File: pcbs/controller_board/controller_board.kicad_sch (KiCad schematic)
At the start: 28 parts, among them J1 A-2014-2-4-N-T-R, J2 PINHD-1X7, J3 PINHD-1X12, J4 PINHD-1X4, P1 PJ-064A, U1 R-78E5.0-1.0, U2 PHOTON2, U3 BSS138, U4 BSS138, U5 BSS138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

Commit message: update controller board to version 0.73
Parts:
- D1: value SS36 -> 3A/60V/750mV; footprint footprints:D_SS36 -> footprints:D_DO-214AB_SMC; symbol symbols:D_SS36 -> symbols:D_Schottky_3A_60V_750mV; DigiKeyURL (none) -> https://www.digikey.com/en/products/detail/onsemi/SS36/1053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; MPN (none) -> SS36; URL https://www.digikey.com/en/products/detail/onsemi/SS36/1053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 -> (none)
- D2: value SS36 -> 1A/40V/500mV; footprint footprints:D_SS36 -> footprints:D_DO-214AC_SMA; symbol symbols:D_SS36 -> symbols:D_Schottky_1A_40V_500mV; DigiKey SS36FSCT-ND -> SS14CT-ND; DigiKeyURL (none) -> https://www.digikey.com/en/products/detail/onsemi/SS14/9654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; MPN (none) -> SS14; URL https://www.digikey.com/en/products/detail/onsemi/SS36/1053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 -> (none)
- D3: value SMBJ36A -> 40V; footprint footprints:TVS_SMBJ36A -> footprints:D_DO-214AA_SMB; symbol symbols:TVS_SMBJ36A -> symbols:D_Zener_40V; DigiKeyURL (none) -> https://www.digikey.com/en/products/detail/littelfuse-inc/S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; MPN (none) -> SMBJ36A; URL https://www.digikey.com/en/products/detail/littelfuse-inc/S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 -> (none)
- F1: value PFSM.075.2 -> 33V/750mA/1.5A; footprint footprints:POLYFUSE_SMD075F-2 -> footprints:Fuse_1812; symbol symbols:Polyfuse_PFSM.075.2 -> symbols:Fuse_33V_750mA_1.5A; DigiKey 486-1176-1-ND -> 118-MF-MSMF075/33X-2CT-ND; DigiKeyURL (none) -> https://www.digikey.com/en/products/detail/bourns-inc/MF-MS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; Info 30V 750 mA -> (none); JLCPCB Datasheet https://jlcpcb.com/api/file/downloadByFileSystemAccessId/85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 -> (none); JLCPCB Part# C70135 -> (none); JLCPCB URL https://jlcpcb.com/partdetail/TECHFUSE-SMD075L/C70135 -> (none); MPN (none) -> MF-MSMF075/33X-2; Type Polyfuse -> (none); URL https://www.digikey.com/en/products/detail/schurter-inc/PFS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 -> (none); UnitPrice (none) -> 0.91
- J1: value A-2014-2-4-N-T-R -> RJ45; footprint footprints:ASSMANN_A-2014-2-4-N-T-R -> footprints:RJ45_A-2014-2-4-N-T-R; DigiKeyURL (none) -> https://www.digikey.com/en/products/detail/assmann-wsw-comp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; MPN (none) -> A-2014-2-4-N-T-R; Type RJ45 -> (none); URL https://www.digikey.com/en/products/detail/assmann-wsw-comp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 -> (none)
- J2: Info OLED-I2C -> (none)
- J3: Info Access-Points -> (none)
- J4: Info V-check -> (none)
- P1: value PJ-064A -> 24V / 5A; DigiKeyURL (none) -> https://www.digikey.com/en/products/detail/cui-devices/PJ-0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; Info Power Supply -> (none); MPN (none) -> PJ-064A; URL https://www.digikey.com/en/products/detail/cui-devices/PJ-0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 -> (none)
- Q1: renamed from U3; value BSS138 -> 220mA / 50V; symbol symbols:BSS138_SOT-23-3 -> symbols:Q_NMOS_220mA_50V; DigiKeyURL (none) -> https://www.digikey.com/en/products/detail/onsemi/BSS138/24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; Info SPEED-shift -> (none); MPN (none) -> BSS138; URL https://www.digikey.com/en/products/detail/onsemi/BSS138/24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 -> (none)
- Q2: renamed from U4; value BSS138 -> 220mA / 50V; symbol symbols:BSS138_SOT-23-3 -> symbols:Q_NMOS_220mA_50V; DigiKeyURL (none) -> https://www.digikey.com/en/products/detail/onsemi/BSS138/24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; Info DECO-shift -> (none); MPN (none) -> BSS138; URL https://www.digikey.com/en/products/detail/onsemi/BSS138/24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 -> (none)
- Q3: renamed from U5; value BSS138 -> 220mA / 50V; symbol symbols:BSS138_SOT-23-3 -> symbols:Q_NMOS_220mA_50V; DigiKeyURL (none) -> https://www.digikey.com/en/products/detail/onsemi/BSS138/24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; Info SCL-shift -> (none); MPN (none) -> BSS138; URL https://www.digikey.com/en/products/detail/onsemi/BSS138/24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 -> (none)
- Q4: renamed from U6; value BSS138 -> 220mA / 50V; symbol symbols:BSS138_SOT-23-3 -> symbols:Q_NMOS_220mA_50V; DigiKeyURL (none) -> https://www.digikey.com/en/products/detail/onsemi/BSS138/24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; Info SDA-shift -> (none); MPN (none) -> BSS138; URL https://www.digikey.com/en/products/detail/onsemi/BSS138/24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 -> (none)
- R1, R10, R11, R12, R13, R14, R2, R3, R4, R5, R6, R8, R9: footprint footprints:R_1206_3216Metric_Pad1.30x1.75mm_HandSolder -> footprints:R_1206
- U1: value R-78E5.0-1.0 -> 8-28V in / 5V 5W out; DigiKeyURL (none) -> https://www.digikey.com/en/products/detail/recom-power/R-78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; Info DC/DC converter -> (none); MPN (none) -> R-78E5.0-1.0; URL https://www.digikey.com/en/products/detail/recom-power/R-78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 -> (none)
- U2: value PHOTON2 -> Particle2 / Boron; Info MCU -> (none); MPN (none) -> PHN2MEA / BRN404; ParticleURL (none) -> https://store.particle.io/collections/wifi/products/photon-2
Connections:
- net +3V3: now also R10.2, R12.2, R14.2; no longer R10.1, R12.1, R14.1
- net +5V: now also R13.1, R8.1, R9.1; no longer R13.2, R8.2, R9.2
- net 5V-DECO: now also R9.2; no longer R9.1
- net 5V-SDA: now also R13.2; no longer R13.1
- net A0-VIN: now also R2.2; no longer R2.1
- net D0-SDA: now also R14.1; no longer R14.2
- net D1-SCL: now also R12.1; no longer R12.2
- net D6-DECO: now also R10.1; no longer R10.2
- net GND: now also R2.1; no longer R2.2
- net at D1.2 (A): now also F1.1; no longer F1.2
- net at Q1.3 (D): now also R8.2; no longer R8.1
- net at P1.1: now also F1.2; no longer F1.1
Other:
- note added: "Access-Points"
- note added: "DC/DC Converter"
- note added: "DECO-shift"
- note added: "Microcontroller"
- note added: "OLED-I2C"
- note added: "Power Supply"
- note added: "SCL-shift"
- note added: "SDA-shift"
- note added: "SPEED-shift"
- note added: "V-check"
- note added: "µLogger Connection"
- moved on the sheet: Q3, R10, R11, R12, R13, R14, R2, R8, R9

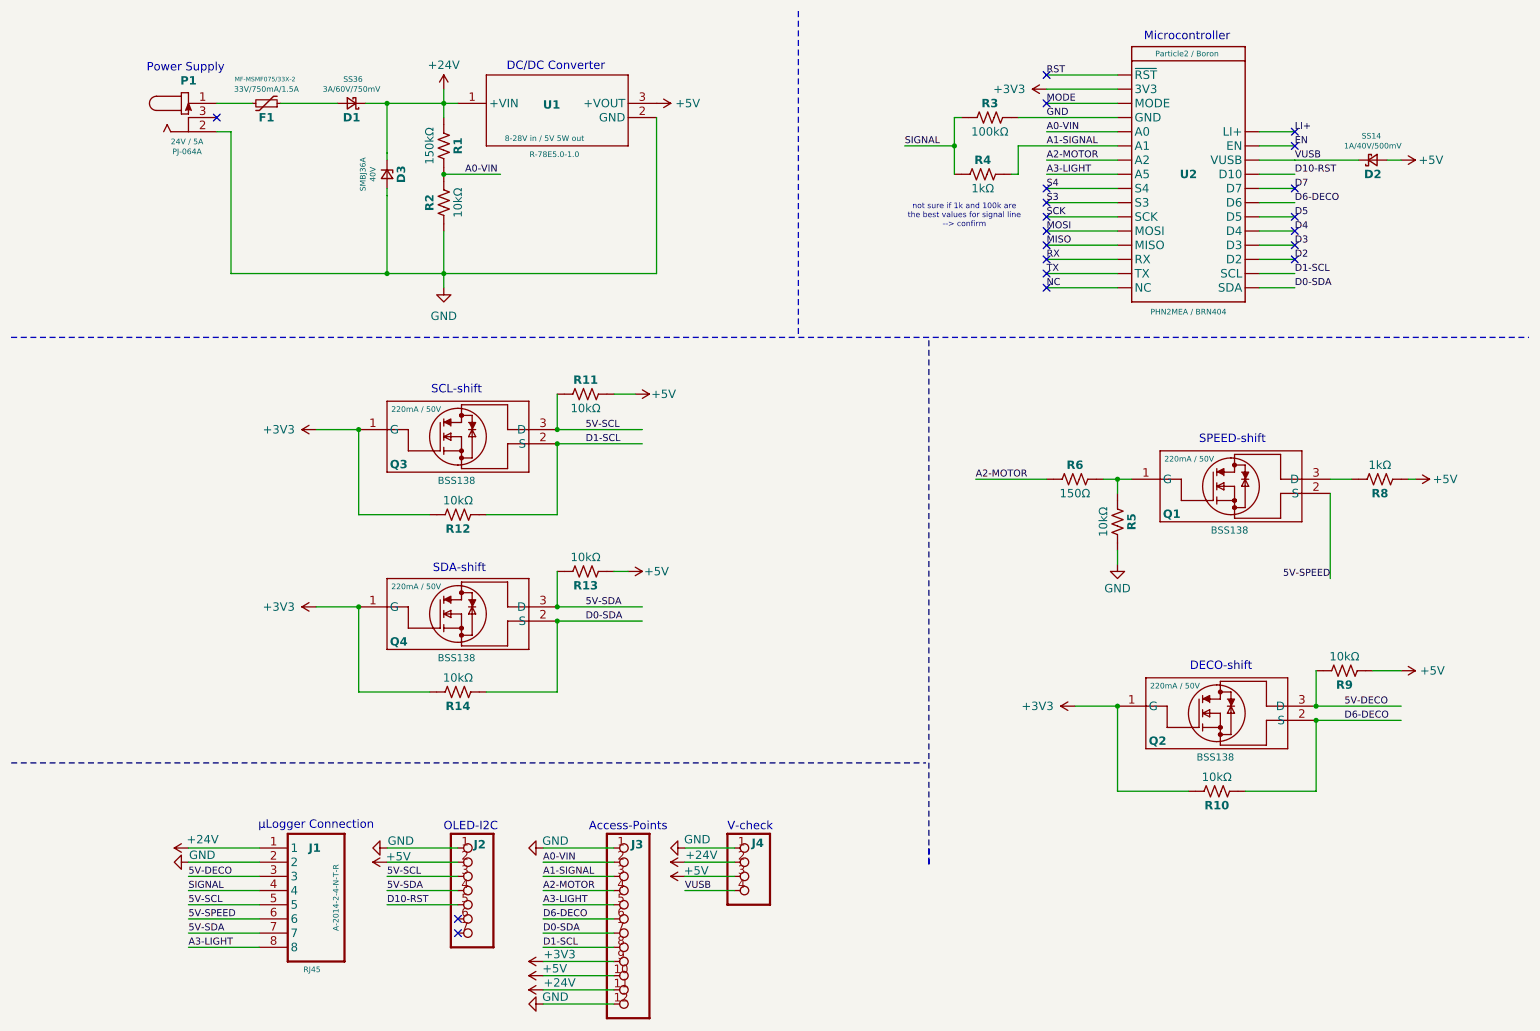
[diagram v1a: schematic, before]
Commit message: update controller board to v0.80
- switch 5V rail to go to device (instead of light output)
- improve protection of 3V/5V I2C bus by using an IC instead of mosfets
- bleed resistor from external 5V to gnd to avoid floating voltage
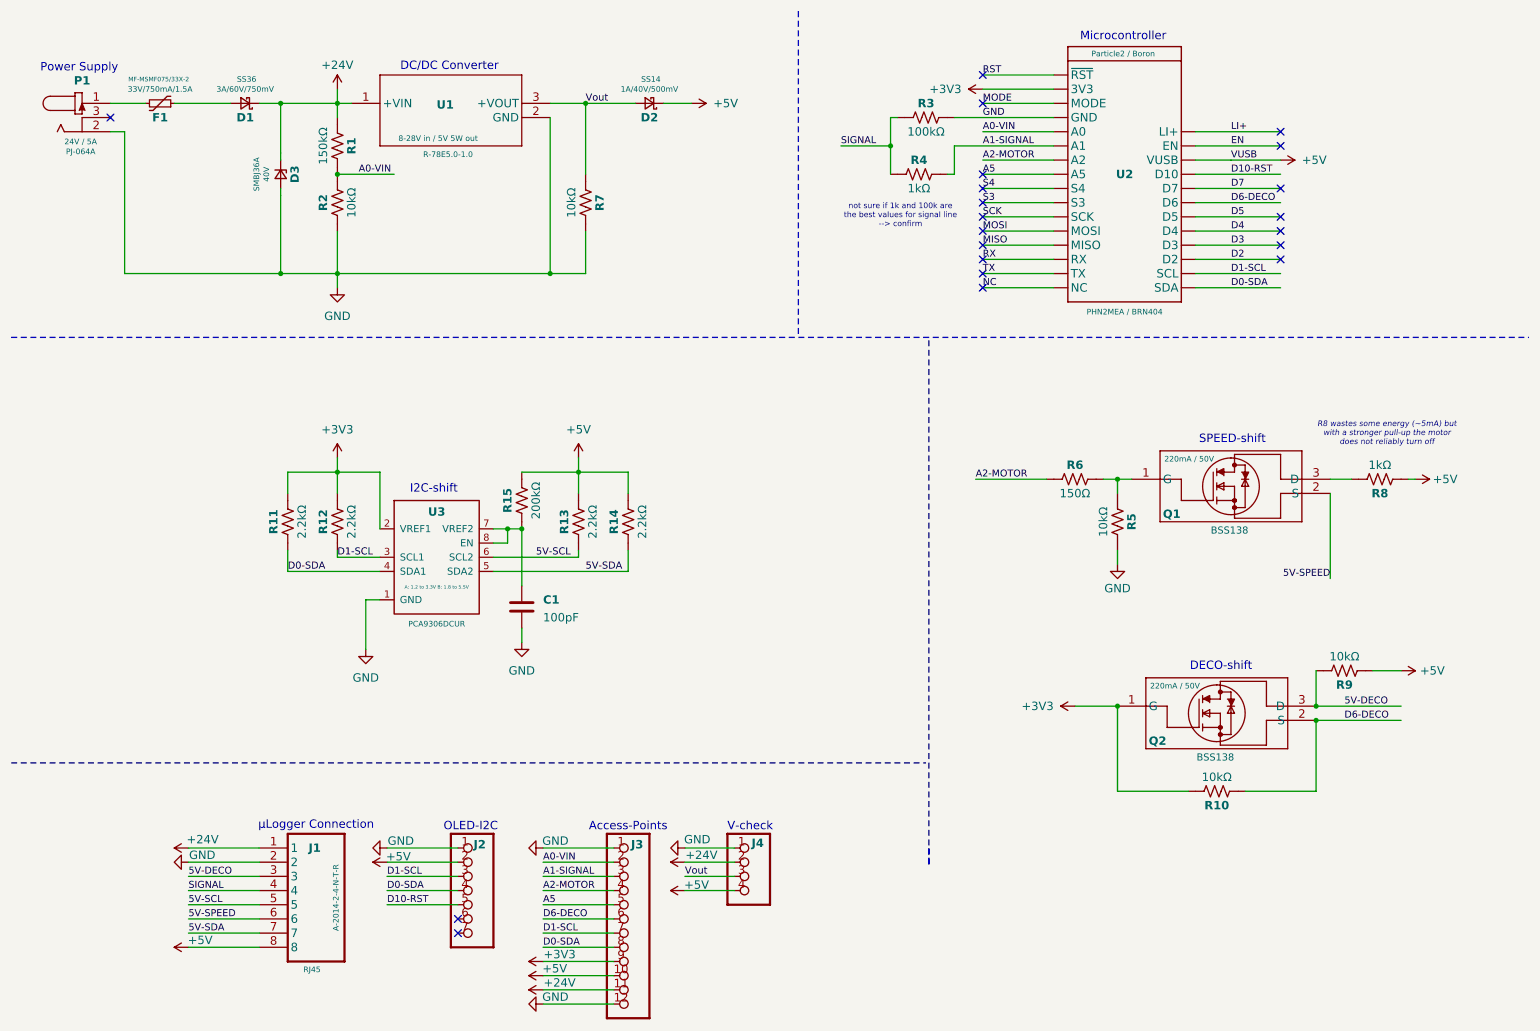
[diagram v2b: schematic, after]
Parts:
- removed Q3, Q4: 220mA / 50V, footprints:SOT-23-3, symbol symbols:Q_NMOS_220mA_50V
- added C1: 100pF, footprints:C_1206, symbol symbols:C
- added R15: 200kΩ, footprints:R_1206, symbol symbols:R_US
- added R7: 10kΩ, footprints:R_1206, symbol symbols:R_US
- added U3: A: 1.2 to 3.3V B: 1.8 to 5.5V, footprints:SOT-765-1_VSSOP8, symbol symbols:PCA9306
- R11, R12, R13, R14: value 10kΩ -> 2.2kΩ
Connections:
- net VUSB is gone; now on net +5V: D2.1 (K), J4.4, U2.26 (VUSB)
- net +3V3: now also R11.2, U3.2 (VREF1); no longer R14.2
- net +5V: now also J1.8, R13.2, R14.2, R15.2; no longer D2.2 (A), J4.3, R11.2, R13.1, U1.3 (+VOUT)
- net 5V-SCL: now also R13.1, U3.6 (SCL2); no longer J2.3, R11.1
- net 5V-SDA: now also R14.1, U3.5 (SDA2); no longer J2.4, R13.2
- net D0-SDA: now also J2.4, J3.8, R11.1, U3.4 (SDA1); no longer J3.7, R14.1
- net D1-SCL: now also J2.3, J3.7, U3.3 (SCL1); no longer J3.8
- net GND: now also C1.2, R7.2, U3.1 (GND)
- net A3-LIGHT renamed A5
- net A5: no longer J1.8
- new net: C1.1, R15.1, U3.7 (VREF2), U3.8 (EN)
- new net Vout: D2.2 (A), J4.3, R7.1, U1.3 (+VOUT)
- no-connect marks 20 -> 21
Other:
- note added: "I2C-shift"
- note added: "R8 wastes some energy (~5mA) but with a stronger pull-up the motor does not reliably turn off"
- note removed: "SCL-shift"
- note removed: "SDA-shift"
- moved on the sheet: D1, D3, F1, P1, R1, R2, R3, R4, U1, U2

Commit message: v 0.81 (removed the 5V on the RJ45)
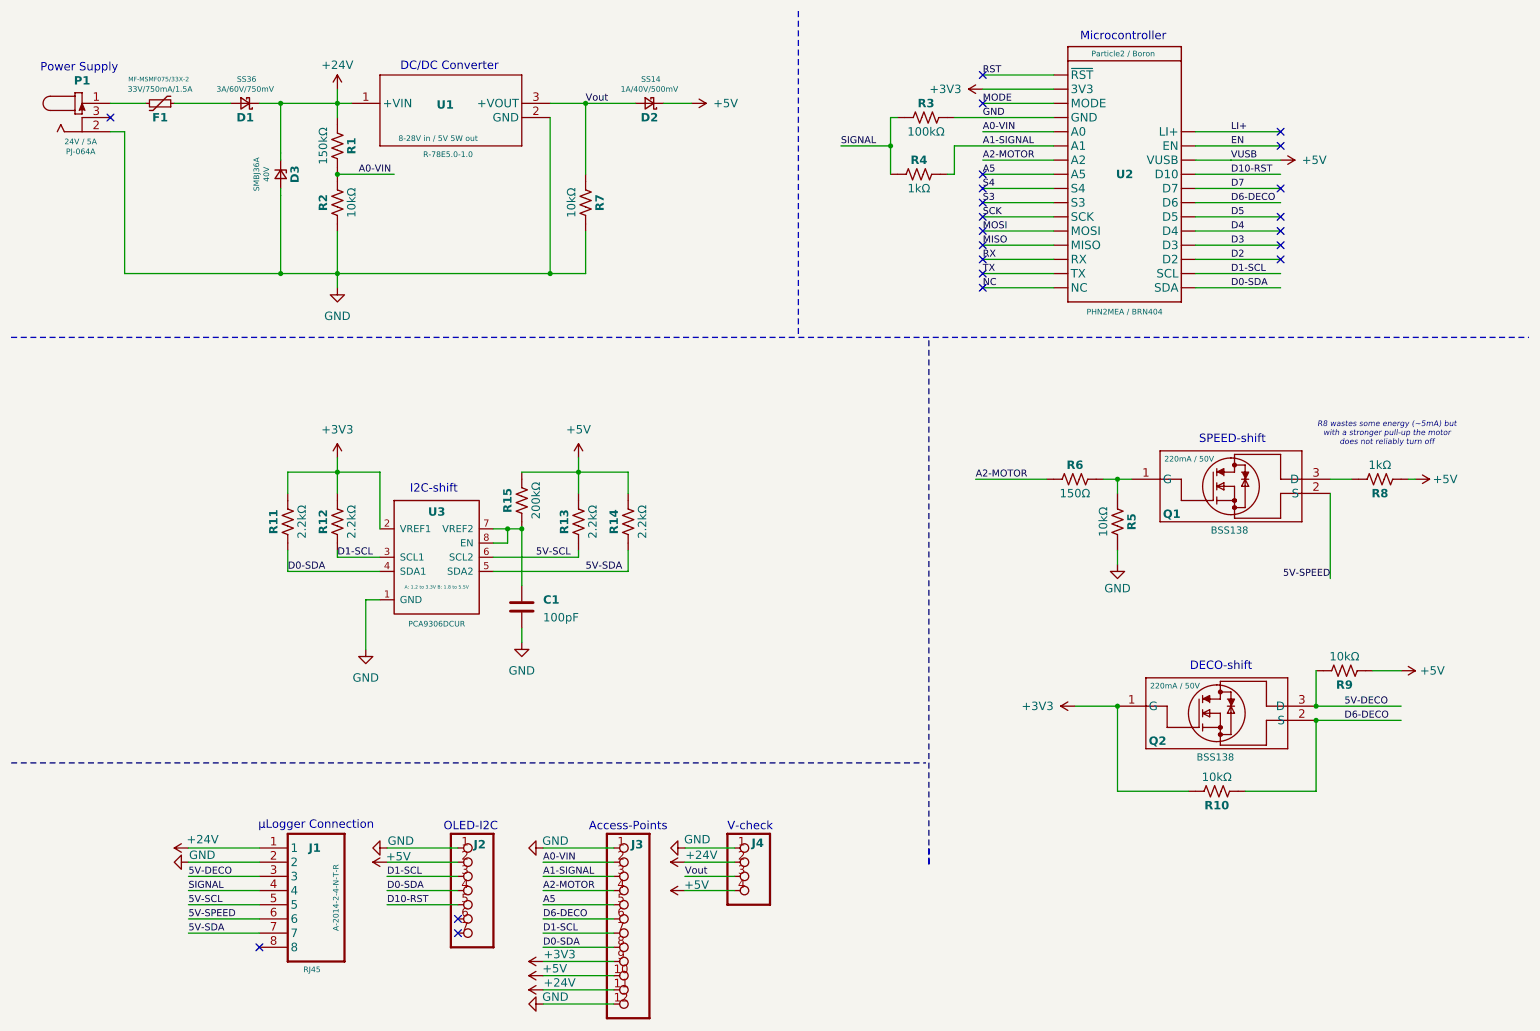
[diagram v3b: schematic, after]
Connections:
- net +5V: no longer J1.8
- no-connect marks 21 -> 22
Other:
- note removed: "not sure if 1k and 100k are the best values for signal line --> confirm"
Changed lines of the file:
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@@
 		)
 	)
-	(text "not sure if 1k and 100k are\nthe best values for signal line\n--> confirm"
-		(exclude_from_sim no)
-		(at 171.958 51.562 0)
-		(effects
-			(font
-				(size 1 1)
-				(color 255 0 0 1)
-			)
-			(justify bottom)
-		)
-	)
 	(text "DC/DC Converter"
 		(exclude_from_sim no)
@@
 	)
 	(no_connect
+		(at 57.15 180.34)
+	)
+	(no_connect
 		(at 186.69 44.45)
 	)
@@
 	(wire
 		(pts
-			(xy 57.15 180.34) (xy 44.45 180.34)
-		)
-		(stroke
-			(width 0.1524)
-			(type solid)
-		)
-	)
-	(wire
-		(pts
 			(xy 57.15 170.18) (xy 44.45 170.18)
 		)
@@
 					(unit 1)
 				)
-			)
-		)
-	)
-	(symbol
-		(lib_id "symbols:+5V")
-		(at 44.45 180.34 90)
-		(unit 1)
-		(exclude_from_sim no)
-		(in_bom yes)
-		(on_board yes)
-		(dnp no)
-		(property "Reference" "#PWR01"
-			(at 48.26 180.34 0)
-			(effects
-				(font
-					(size 1.27 1.27)
-				)
-				(hide yes)
-			)
-		)
-		(property "Value" "+5V"
-			(at 48.768 179.07 90)
-			(effects
-				(font
-					(size 1.5 1.5)
-				)
-				(justify left)
-			)
-		)
-		(property "Footprint" ""
-			(at 44.45 180.34 0)
-			(effects
-				(font
-					(size 1.27 1.27)
-				)
-				(hide yes)
-			)
-		)
-		(property "Datasheet" ""
-			(at 44.45 180.34 0)
-			(effects
-				(font
-					(size 1.27 1.27)
-				)
-				(hide yes)
-			)
-		)
-		(property "Description" "Power symbol creates a global label with name \"+5V\""
-			(at 44.45 180.34 0)
-			(effects
-				(font
-					(size 1.27 1.27)
-				)
-				(hide yes)
-			)
-		)
-		(pin "1"
-		)
-		(instances
-			(project ""
-				(path "/ba44af6b-d897-4c95-8815-b8860eb38091"
-					(reference "#PWR01")
-					(unit 1)
-				)

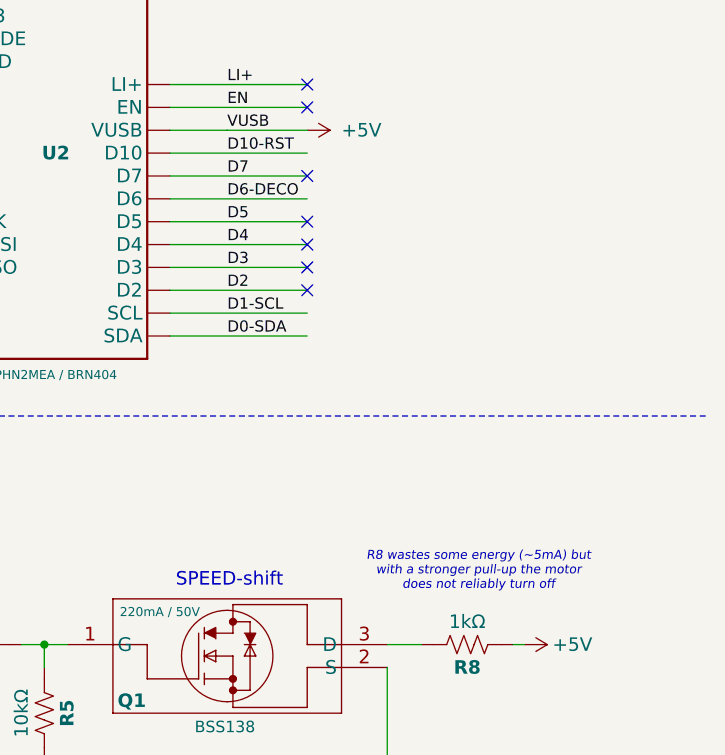
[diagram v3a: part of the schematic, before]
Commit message: include board version information (version 1.0)
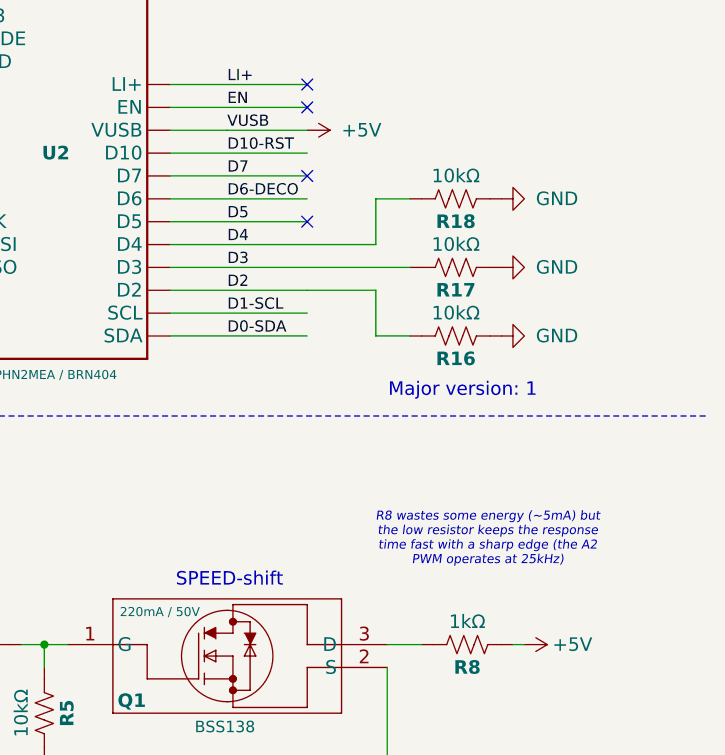
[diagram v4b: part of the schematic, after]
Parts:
- added R16, R17, R18: 10kΩ, footprints:R_1206, symbol symbols:R_US
- D1: JLCPCB (none) -> C391251; JLCPCBURL (none) -> https://jlcpcb.com/partdetail/onsemi-SS36/C391251
- D2: JLCPCB (none) -> C83852; JLCPCBURL (none) -> https://jlcpcb.com/partdetail/onsemi-SS14/C83852
- D3: JLCPCB (none) -> C224020; JLCPCBURL (none) -> https://jlcpcb.com/partdetail/Littelfuse-SMBJ36A/C224020
- F1: JLCPCB (none) -> C3760814; JLCPCBURL (none) -> https://jlcpcb.com/partdetail/BOURNS-MF_MSMF075_33X2/C37608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; UnitPrice 0.91 -> (none)
- Q1, Q2: JLCPCB (none) -> C52895; JLCPCBURL (none) -> https://jlcpcb.com/partdetail/onsemi-BSS138/C52895
- R1: JLCPCB (none) -> C17916; JLCPCBURL (none) -> https://jlcpcb.com/partdetail/18604-1206W4F1503T5E/C17916
- R11: JLCPCB (none) -> C17948; JLCPCBURL (none) -> https://jlcpcb.com/partdetail/18636-1206W4F2201T5E/C17948
- R15: JLCPCB (none) -> C17954; JLCPCBURL (none) -> https://jlcpcb.com/partdetail/18642-1206W4F2003T5E/C17954
- R3: JLCPCB (none) -> C17900; JLCPCBURL (none) -> https://jlcpcb.com/partdetail/18588-1206W4F1003T5E/C17900
- R5: JLCPCB (none) -> C17902; JLCPCBURL (none) -> https://jlcpcb.com/partdetail/18590-1206W4F1002T5E/C17902
- R6: JLCPCB (none) -> C17917; JLCPCBURL (none) -> https://jlcpcb.com/partdetail/18605-1206W4F1500T5E/C17917
- R8: JLCPCB (none) -> C4410; JLCPCBURL (none) -> https://jlcpcb.com/partdetail/4817-1206W4F1001T5E/C4410
- U3: symbol symbols:PCA9306 -> symbols:LevelShifter_PCA9306; JLCPCB (none) -> C33196; JLCPCBURL (none) -> https://jlcpcb.com/partdetail/TexasInstruments-PCA9306DCUR/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
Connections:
- net D2: now also R16.2
- net D3: now also R17.2
- net D4: now also R18.2
- net GND: now also R16.1, R17.1, R18.1
- no-connect marks 22 -> 19
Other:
- note added: "Major version: 1"
- note added: "R8 wastes some energy (~5mA) but the low resistor keeps the response time fast with a sharp edge (the A2 PWM operates at 25kHz)"
- note removed: "R8 wastes some energy (~5mA) but with a stronger pull-up the motor does not reliably turn off"
